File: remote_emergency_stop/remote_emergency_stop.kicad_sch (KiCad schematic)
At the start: 22 parts, among them J1 Conn_01x02, J2 Conn_01x02, J3 Conn_01x02, Q1 BSS138, SW1 SW_DIP_x02, U1 MOUDLE-SEEEDUINO-XIAO-ESP32C3

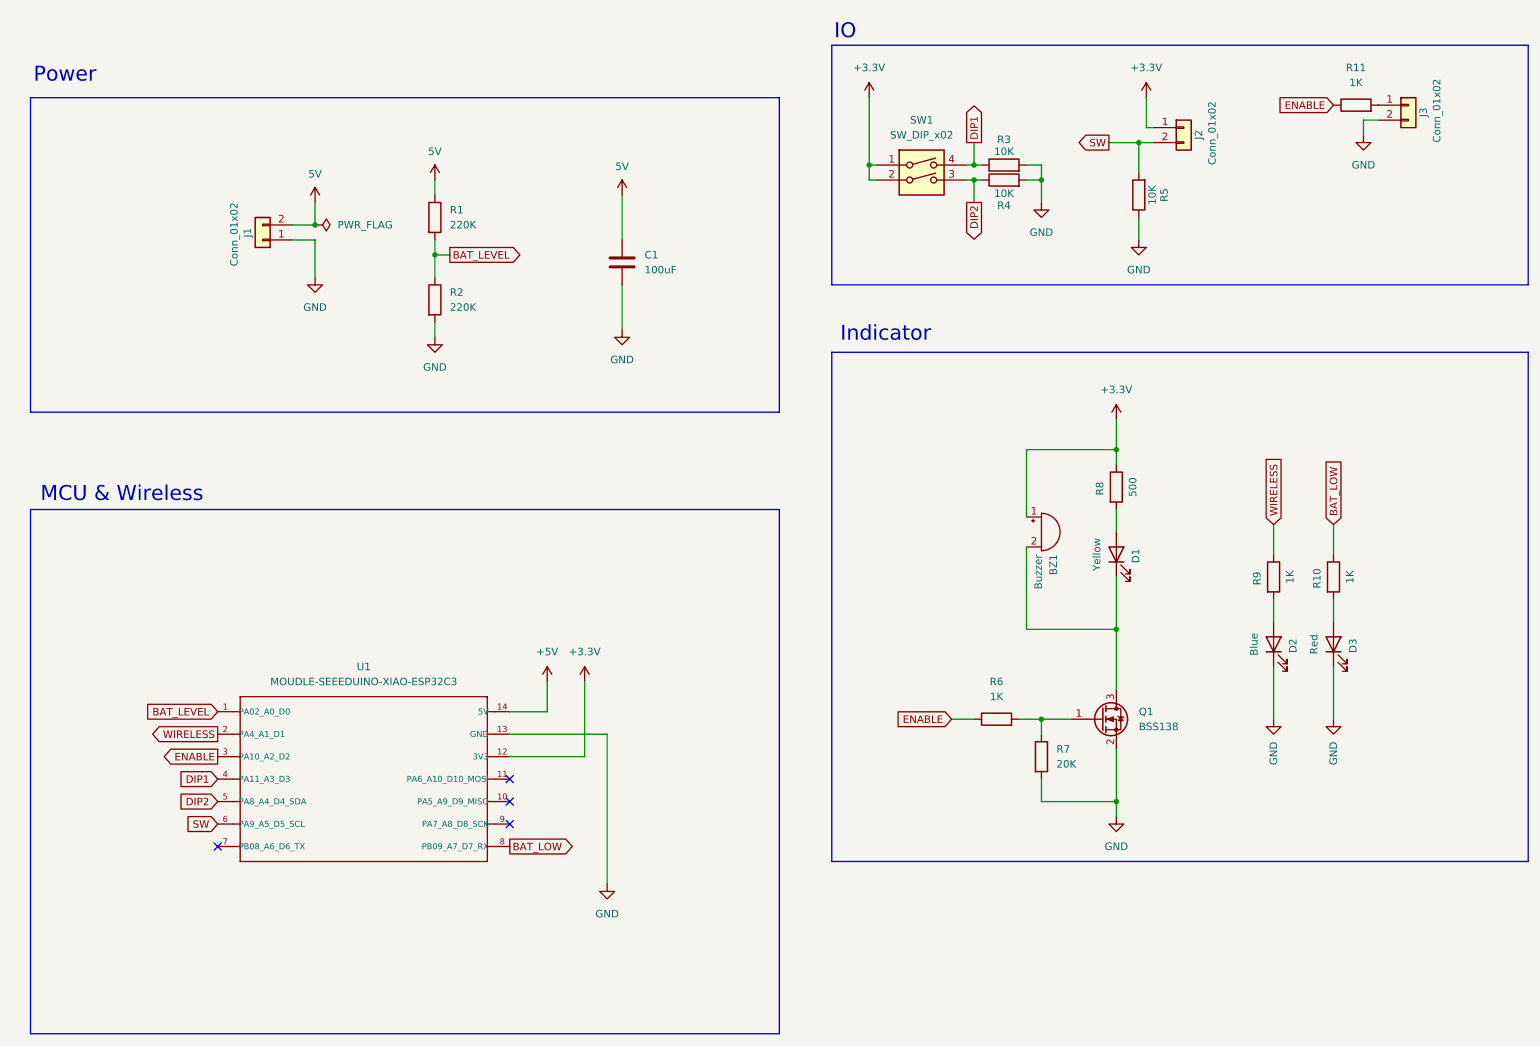
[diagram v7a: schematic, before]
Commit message: STM32のピン配置とインジケーターを追加
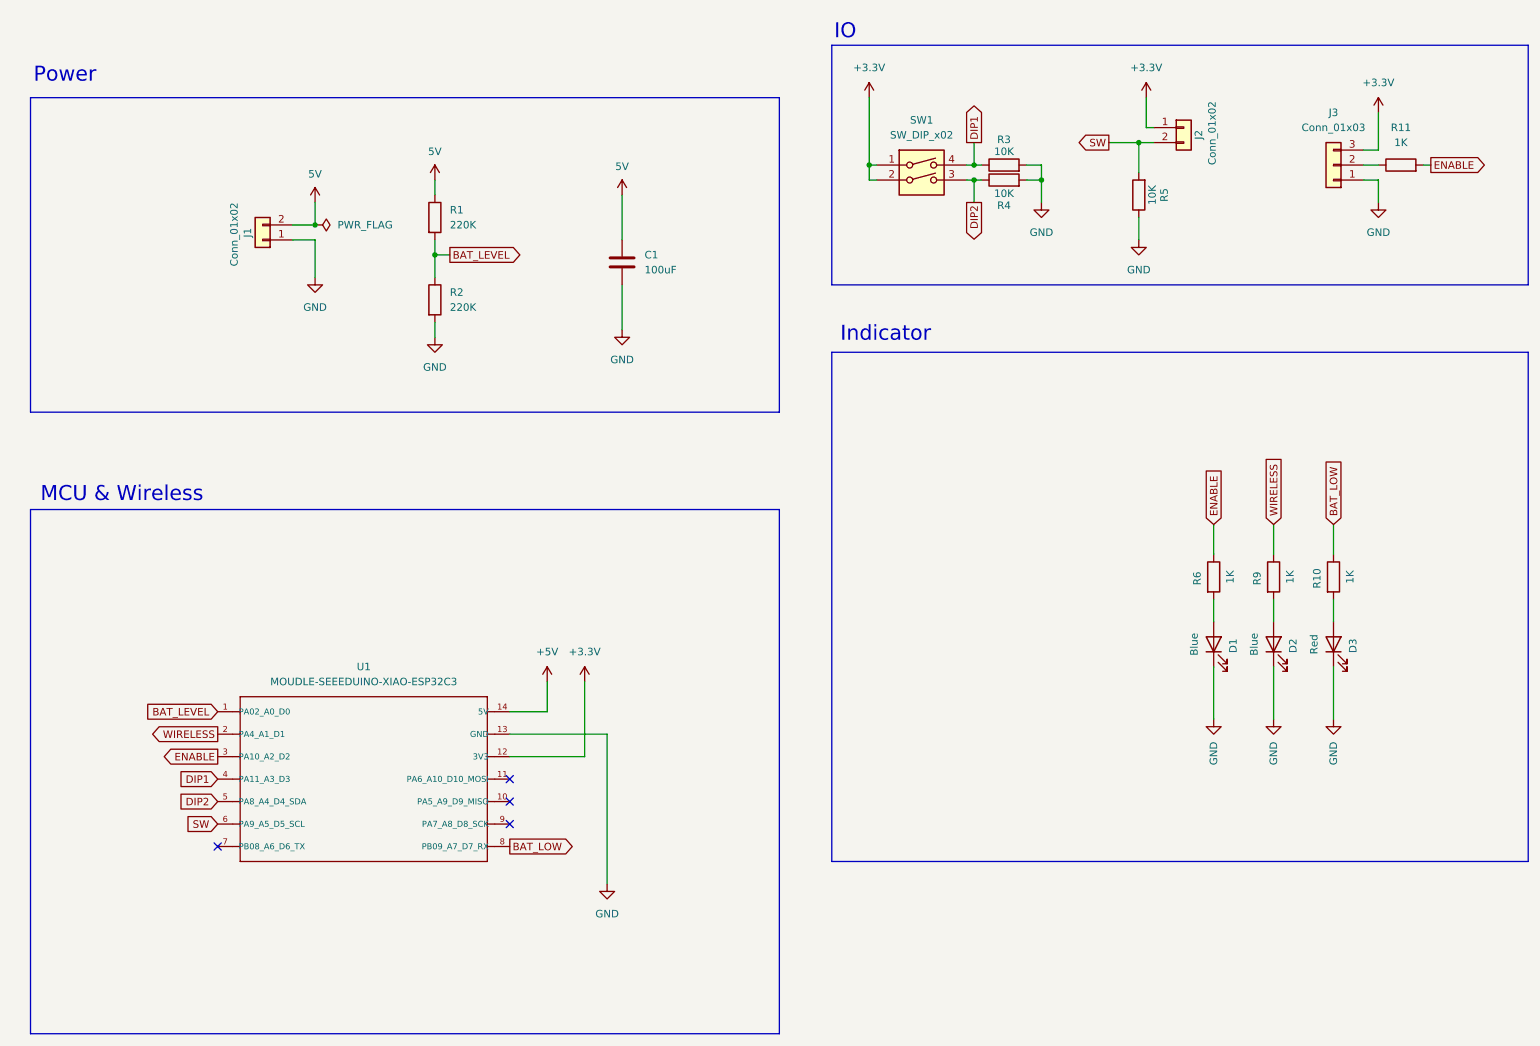
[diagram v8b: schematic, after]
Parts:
- removed BZ1: Buzzer, Buzzer_Beeper:Buzzer_12x9.5RM7.6, symbol Device:Buzzer
- removed J3: Conn_01x02, Connector_JST:JST_XH_S2B-XH-A_1x02_P2.50mm_Horizontal, symbol Connector_Generic:Conn_01x02
- removed Q1: BSS138, Package_TO_SOT_SMD:SOT-23, symbol Transistor_FET:AO3400A
- removed R7: 20K, Resistor_SMD:R_0603_1608Metric, symbol Device:R
- removed R8: 500, Resistor_SMD:R_0603_1608Metric, symbol Device:R
- added J3: Conn_01x03, symbol Connector_Generic:Conn_01x03
- D1: value Yellow -> Blue
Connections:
- net +3.3V: now also J3.3 (Pin_3)
- net ENABLE: now also R11.2; no longer R11.1
- net GND: now also D1.1 (K), J3.1 (Pin_1)
- net at R6.2: now also D1.2 (A)
- new net: J3.2 (Pin_2), R11.1
